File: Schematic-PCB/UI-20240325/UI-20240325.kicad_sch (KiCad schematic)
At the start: 18 parts, among them J1 Conn_01x10_Pin, SW1 SW_SPDT, SW2 SW_SPDT, SW3 SW_Push, SW5 SW_Push

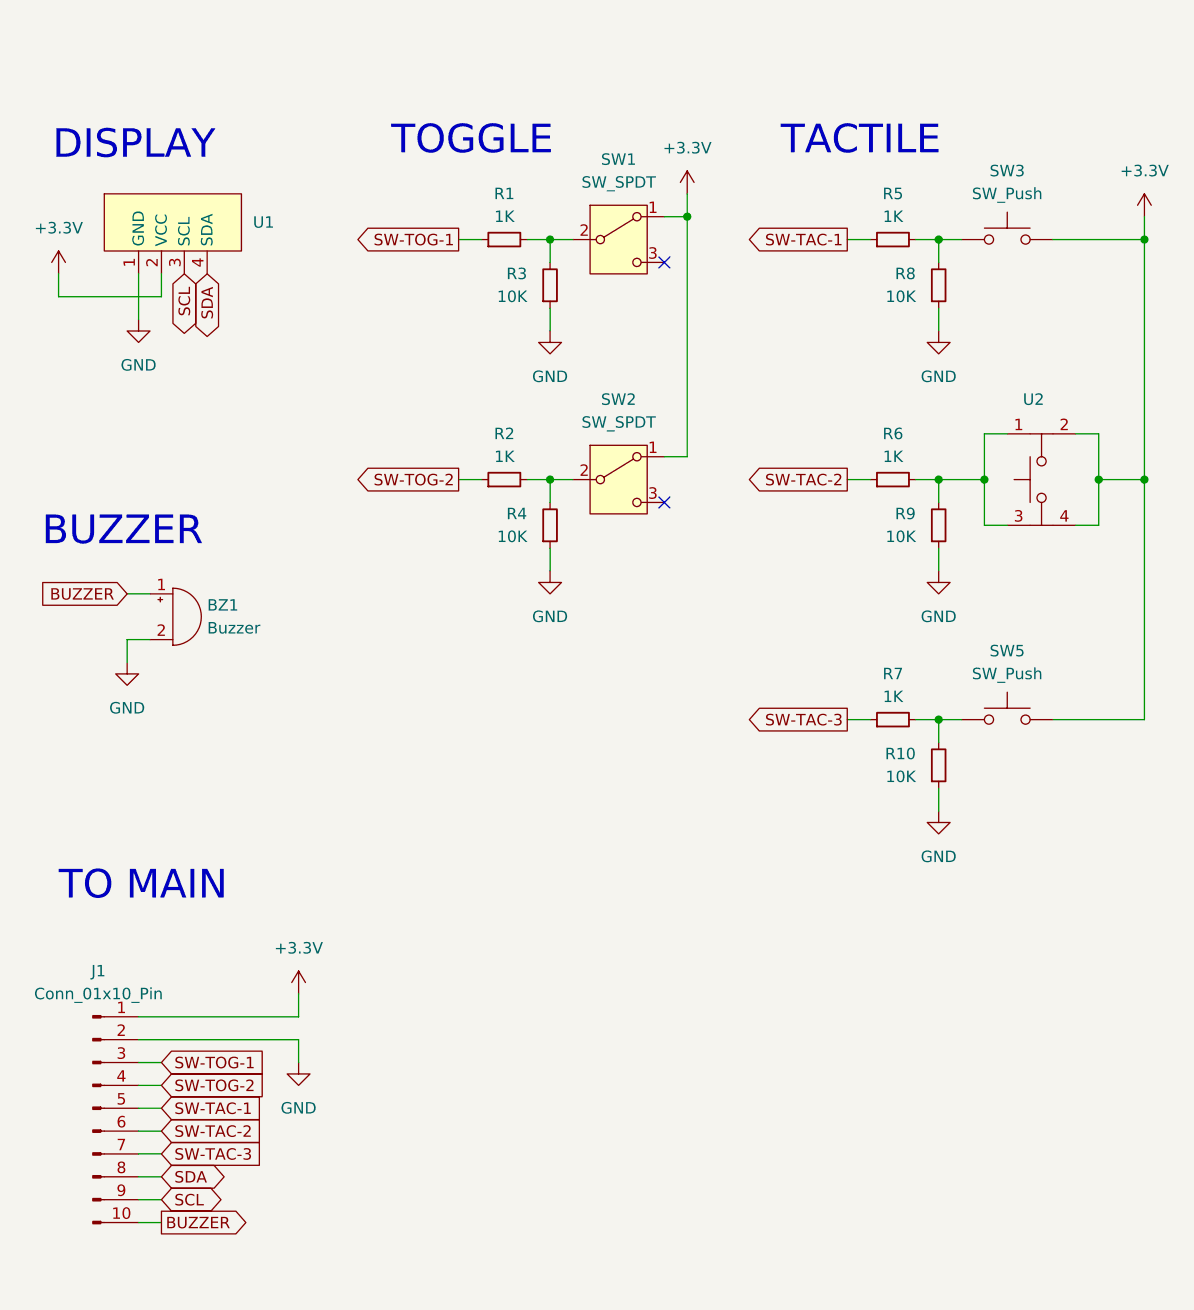
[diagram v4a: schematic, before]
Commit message: UI基板の回路図とPCBを作成しなおした
DRよろしく
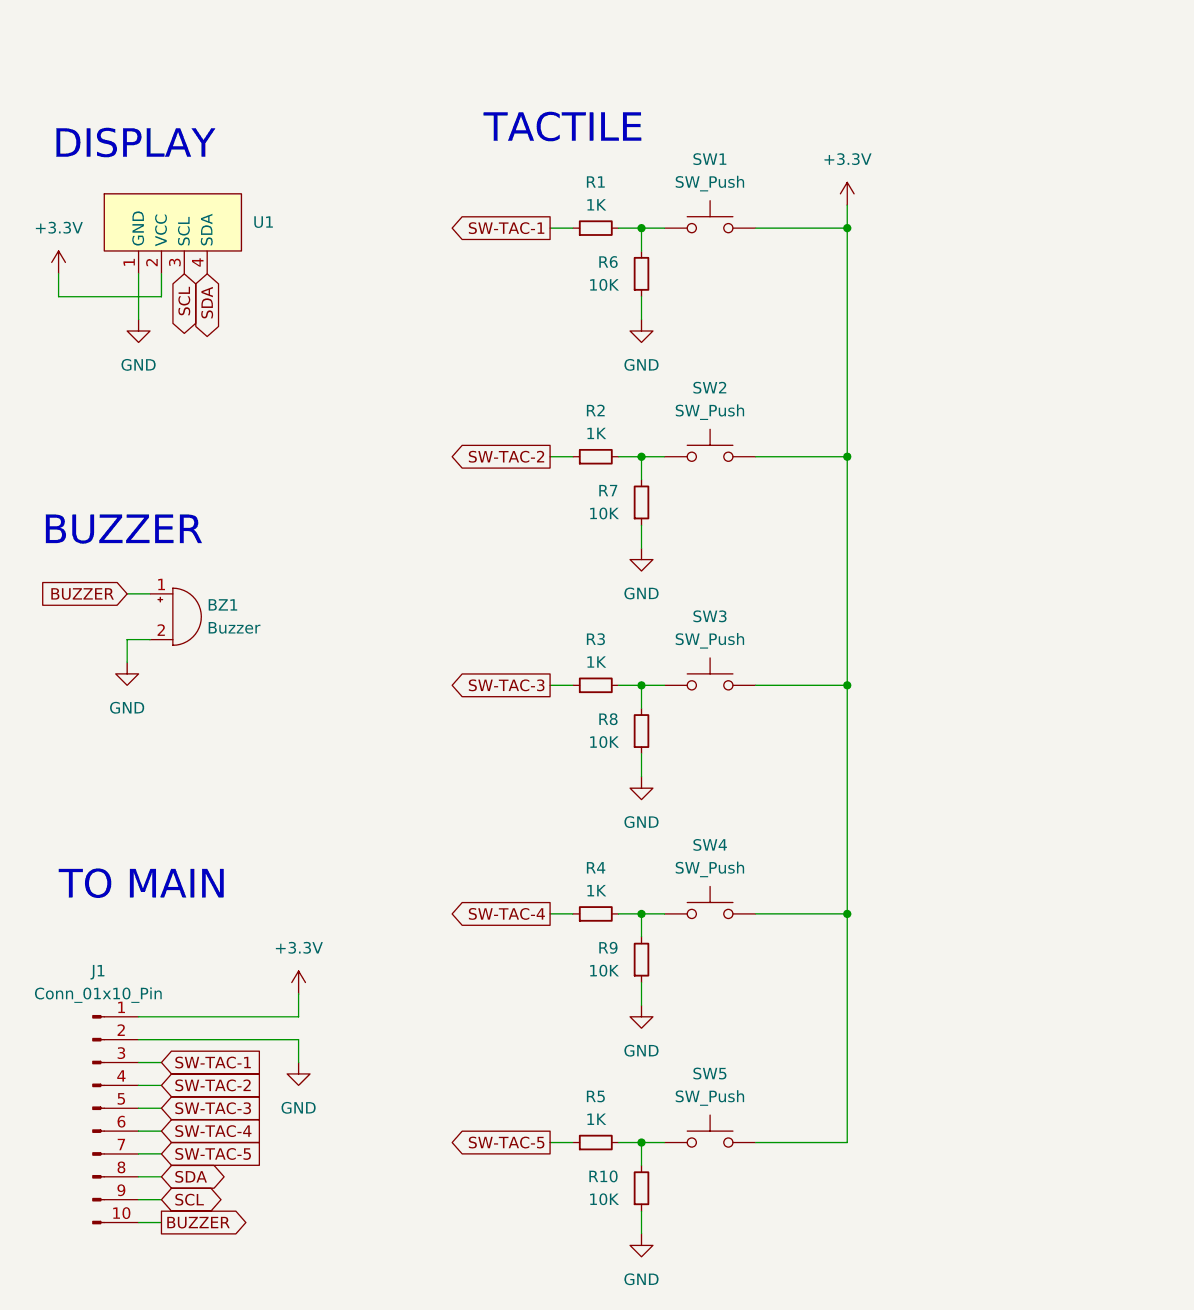
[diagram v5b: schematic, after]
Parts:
- removed R1, R6: 1K, Resistor_SMD:R_0603_1608Metric, symbol Device:R_Small
- removed SW1, SW2: SW_SPDT, @2024-UI:2MS1-T1-B4-VS2-Q-E-S, symbol Switch:SW_SPDT
- removed U2: ~, @2024-UI:TVGP01-G73BB, symbol @2024-UI:TVGP01-G73BB
- added R5: 1K, Resistor_SMD:R_0603_1608Metric, symbol Device:R_Small
- added R8: 10K, Resistor_SMD:R_0603_1608Metric, symbol Device:R_Small
- added SW2, SW3, SW4: SW_Push, @2024-UI:TVBP06-B043C, symbol Switch:SW_Push
- R3, R4: value 10K -> 1K
- R7: value 1K -> 10K
- renumbered R5 to R1, R8 to R6, SW3 to SW1
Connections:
- net SW-TOG-1 is gone; now on net SW-TAC-1: J1.3 (Pin_3)
- net SW-TOG-2 is gone; now on net SW-TAC-2: J1.4 (Pin_4), R2.1
- net +3.3V: now also SW2.2, SW3.2, SW4.2
- net GND: now also R7.1, R8.1; no longer R3.1, R4.1
- net SW-TAC-1: no longer J1.5 (Pin_5)
- net SW-TAC-2: no longer J1.6 (Pin_6)
- net SW-TAC-3: now also J1.5 (Pin_5), R3.1; no longer J1.7 (Pin_7), R7.1
- net at R10.2, SW5.1: now also R5.2; no longer R7.2
- net at R3.2: now also R8.2, SW3.1
- net at R2.2: now also R7.2, SW2.1; no longer R4.2
- net at R9.2: now also R4.2, SW4.1
- new net SW-TAC-4: J1.6 (Pin_6), R4.1
- new net SW-TAC-5: J1.7 (Pin_7), R5.1
- no-connect marks 2 -> 0
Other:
- note removed: "TOGGLE"
- moved on the sheet: R1, R6, SW1

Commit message: ラインセンサ基板のPCBを更新
ちょっと停滞中... ヘルプ求む、
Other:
- moved on the sheet: BZ1, J1, R1, R10, R2, R3, R4, R5, R6, R7, R8, R9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

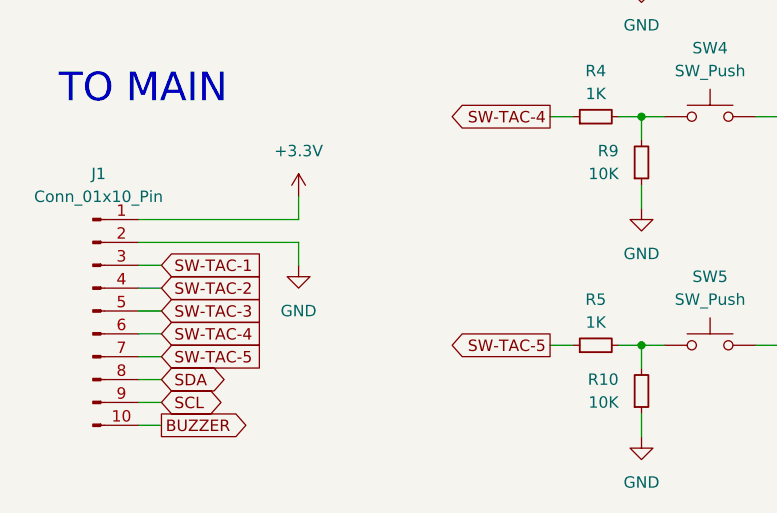
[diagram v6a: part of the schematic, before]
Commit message: UI基板の配線がねじれてしまう問題を解決した
ピンアサインに変更有、ピンアサイン図の変更が必要
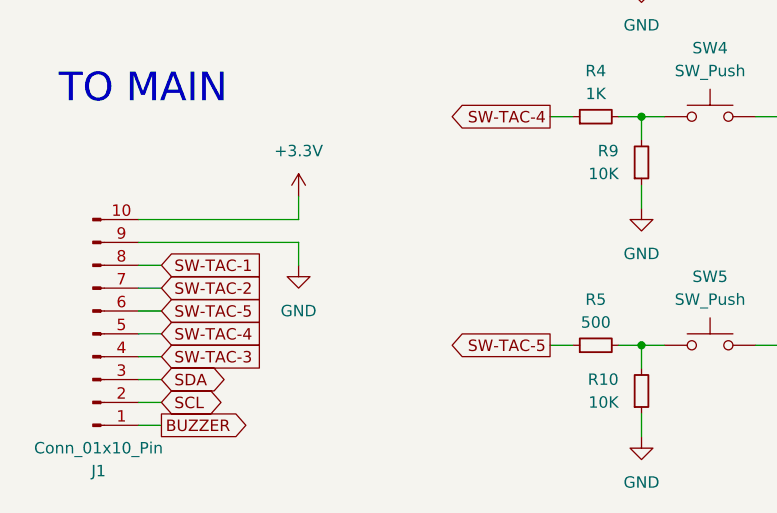
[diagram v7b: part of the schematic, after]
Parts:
- BZ1: footprint @2024-UI:PKM13EPYH4000-A0 -> @2024TOINIOT2-UI:PKM13EPYH4000-A0
- R5: value 1K -> 500
- SW1, SW2, SW3, SW4, SW5: footprint @2024-UI:TVBP06-B043C -> @2024TOINIOT2-UI:TVBP06-B043C
- U1: footprint @2024-UI:Display -> @2024TOINIOT2-UI:Display
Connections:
- net +3.3V: now also J1.10 (Pin_10); no longer J1.1 (Pin_1)
- net BUZZER: now also J1.1 (Pin_1); no longer J1.10 (Pin_10)
- net GND: now also J1.9 (Pin_9); no longer J1.2 (Pin_2)
- net SCL: now also J1.2 (Pin_2); no longer J1.9 (Pin_9)
- net SDA: now also J1.3 (Pin_3); no longer J1.8 (Pin_8)
- net SW-TAC-1: now also J1.8 (Pin_8); no longer J1.3 (Pin_3)
- net SW-TAC-2: now also J1.7 (Pin_7); no longer J1.4 (Pin_4)
- net SW-TAC-3: now also J1.4 (Pin_4); no longer J1.5 (Pin_5)
- net SW-TAC-4: now also J1.5 (Pin_5); no longer J1.6 (Pin_6)
- net SW-TAC-5: now also J1.6 (Pin_6); no longer J1.7 (Pin_7)
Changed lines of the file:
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@@
 	(global_label "SW-TAC-5"
 		(shape input)
-		(at 43.18 143.51 0)
+		(at 43.18 138.43 0)
 		(fields_autoplaced yes)
 		(effects
@@
 		)
 		(property "Intersheetrefs" "${INTERSHEET_REFS}"
-			(at 55.2496 143.51 0)
+			(at 55.2496 138.43 0)
 			(effects
 				(font
@@
 	(global_label "SW-TAC-3"
 		(shape input)
-		(at 43.18 138.43 0)
+		(at 43.18 143.51 0)
 		(fields_autoplaced yes)
 		(effects
@@
 		)
 		(property "Intersheetrefs" "${INTERSHEET_REFS}"
-			(at 55.2496 138.43 0)
+			(at 55.2496 143.51 0)
 			(effects
 				(font
@@
 			)
 		)
-		(property "Footprint" "@2024-UI:TVBP06-B043C"
+		(property "Footprint" "@2024TOINIOT2-UI:TVBP06-B043C"
 			(at 104.14 35.56 0)
 			(effects
@@
 			)
 		)
-		(property "Footprint" "@2024-UI:TVBP06-B043C"
+		(property "Footprint" "@2024TOINIOT2-UI:TVBP06-B043C"
 			(at 104.14 137.16 0)
 			(effects
@@
 	(symbol
 		(lib_id "Connector:Conn_01x10_Pin")
-		(at 35.56 138.43 0)
-		(unit 1)
-		(exclude_from_sim no)
-		(in_bom yes)
-		(on_board yes)
-		(dnp no)
-		(fields_autoplaced yes)
+		(at 35.56 140.97 0)
+		(mirror x)
+		(unit 1)
+		(exclude_from_sim no)
+		(in_bom yes)
+		(on_board yes)
+		(dnp no)
 		(property "Reference" "J1"
-			(at 36.195 123.19 0)
+			(at 36.195 156.21 0)
 			(effects
 				(font
@@
 		)
 		(property "Value" "Conn_01x10_Pin"
-			(at 36.195 125.73 0)
+			(at 36.195 153.67 0)
 			(effects
 				(font
@@
 		)
 		(property "Footprint" "Connector_JST:JST_XH_B10B-XH-A_1x10_P2.50mm_Vertical"
-			(at 35.56 138.43 0)
+			(at 35.56 140.97 0)
 			(effects
 				(font
@@
 		)
 		(property "Datasheet" "~"
-			(at 35.56 138.43 0)
+			(at 35.56 140.97 0)
 			(effects
 				(font
@@
 		)
 		(property "Description" "Generic connector, single row, 01x10, script generated"
-			(at 35.56 138.43 0)
+			(at 35.56 140.97 0)
 			(effects
 				(font
@@
 			)
 		)
-		(property "Footprint" "@2024-UI:Display"
+		(property "Footprint" "@2024TOINIOT2-UI:Display"
 			(at 44.45 29.718 0)
 			(effects
@@
 			)
 		)
-		(property "Footprint" "@2024-UI:TVBP06-B043C"
+		(property "Footprint" "@2024TOINIOT2-UI:TVBP06-B043C"
 			(at 104.14 86.36 0)
 			(effects
@@
 			)
 		)
-		(property "Footprint" "@2024-UI:PKM13EPYH4000-A0"
+		(property "Footprint" "@2024TOINIOT2-UI:PKM13EPYH4000-A0"
 			(at 43.815 81.28 90)
 			(effects
@@
 			)
 		)
-		(property "Footprint" "@2024-UI:TVBP06-B043C"
+		(property "Footprint" "@2024TOINIOT2-UI:TVBP06-B043C"
 			(at 104.14 60.96 0)
 			(effects
@@
 			)
 		)
-		(property "Value" "1K"
+		(property "Value" "500"
 			(at 91.44 139.7 90)
 			(effects
@@
 			)
 		)
-		(property "Footprint" "@2024-UI:TVBP06-B043C"
+		(property "Footprint" "@2024TOINIOT2-UI:TVBP06-B043C"
 			(at 104.14 111.76 0)
 			(effects

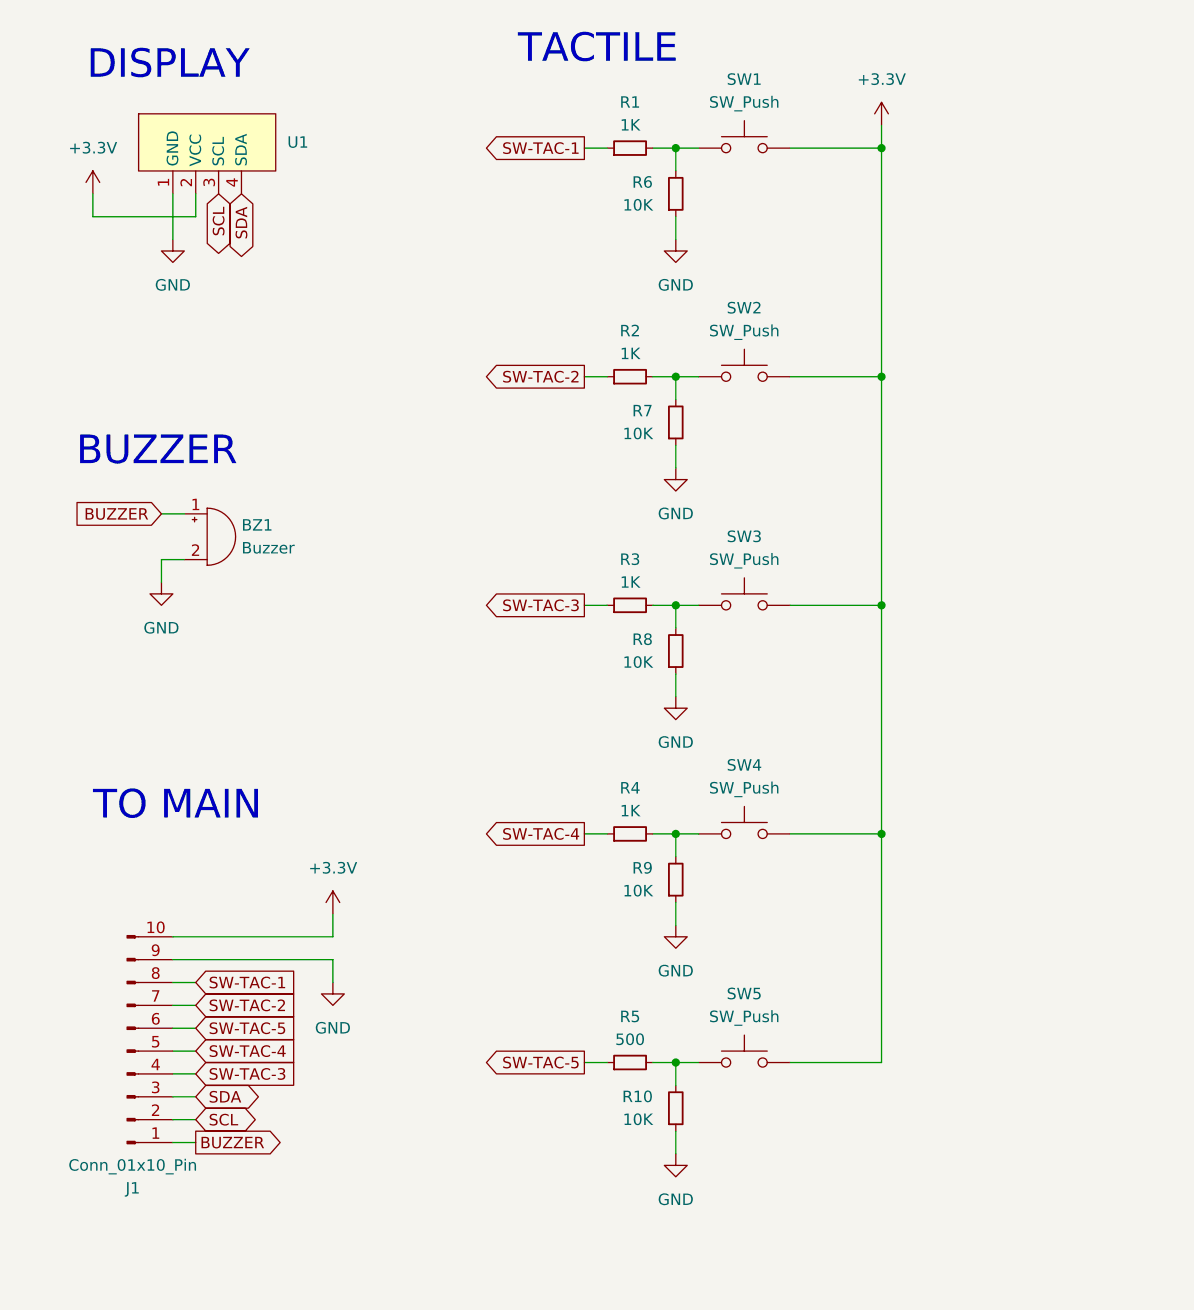
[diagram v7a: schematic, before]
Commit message: UI基板を修正/MD基板を修正/メイン基板を作り直し （ver.002）
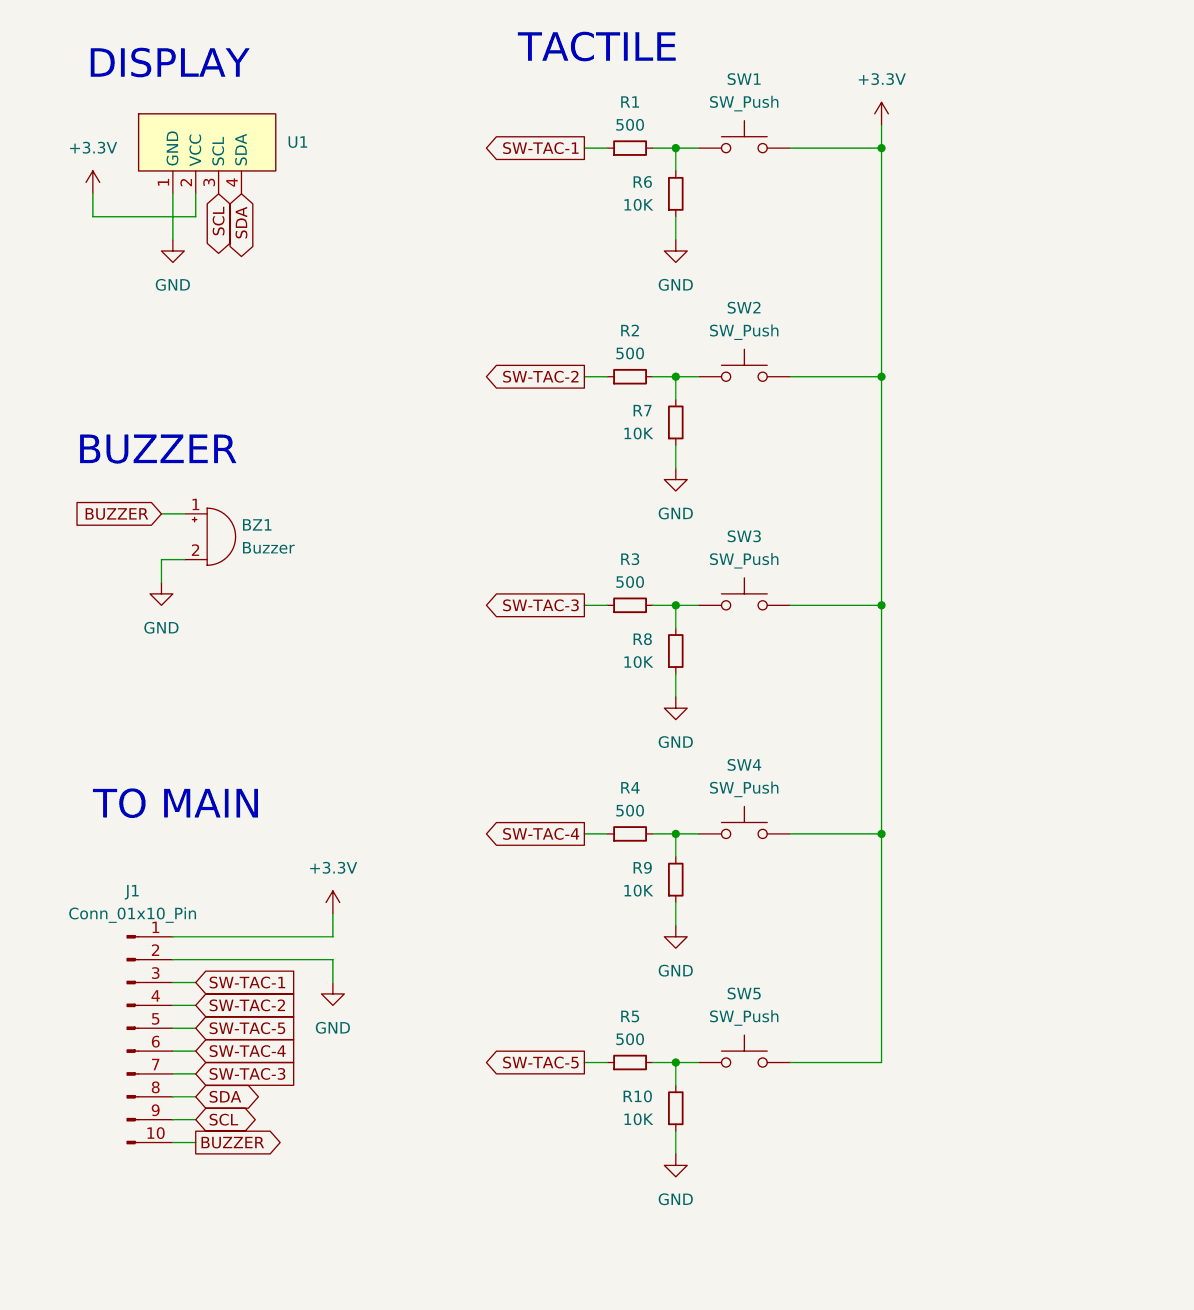
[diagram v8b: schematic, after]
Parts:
- R1, R2, R3, R4: value 1K -> 500
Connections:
- net +3.3V: now also J1.1 (Pin_1); no longer J1.10 (Pin_10)
- net BUZZER: now also J1.10 (Pin_10); no longer J1.1 (Pin_1)
- net GND: now also J1.2 (Pin_2); no longer J1.9 (Pin_9)
- net SCL: now also J1.9 (Pin_9); no longer J1.2 (Pin_2)
- net SDA: now also J1.8 (Pin_8); no longer J1.3 (Pin_3)
- net SW-TAC-1: now also J1.3 (Pin_3); no longer J1.8 (Pin_8)
- net SW-TAC-2: now also J1.4 (Pin_4); no longer J1.7 (Pin_7)
- net SW-TAC-3: now also J1.7 (Pin_7); no longer J1.4 (Pin_4)
- net SW-TAC-4: now also J1.6 (Pin_6); no longer J1.5 (Pin_5)
- net SW-TAC-5: now also J1.5 (Pin_5); no longer J1.6 (Pin_6)
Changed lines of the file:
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@@
 			)
 		)
-		(property "Value" "1K"
+		(property "Value" "500"
 			(at 91.44 38.1 90)
 			(effects
@@
 			)
 		)
-		(property "Value" "1K"
+		(property "Value" "500"
 			(at 91.44 88.9 90)
 			(effects
@@
 	(symbol
 		(lib_id "Connector:Conn_01x10_Pin")
-		(at 35.56 140.97 0)
-		(mirror x)
+		(at 35.56 138.43 0)
 		(unit 1)
 		(exclude_from_sim no)
@@
 		(dnp no)
 		(property "Reference" "J1"
-			(at 36.195 156.21 0)
+			(at 36.195 123.19 0)
 			(effects
 				(font
@@
 		)
 		(property "Value" "Conn_01x10_Pin"
-			(at 36.195 153.67 0)
+			(at 36.195 125.73 0)
 			(effects
 				(font
@@
 		)
 		(property "Footprint" "Connector_JST:JST_XH_B10B-XH-A_1x10_P2.50mm_Vertical"
-			(at 35.56 140.97 0)
+			(at 35.56 138.43 0)
 			(effects
 				(font
@@
 		)
 		(property "Datasheet" "~"
-			(at 35.56 140.97 0)
+			(at 35.56 138.43 0)
 			(effects
 				(font
@@
 		)
 		(property "Description" "Generic connector, single row, 01x10, script generated"
-			(at 35.56 140.97 0)
+			(at 35.56 138.43 0)
 			(effects
 				(font
@@
 			)
 		)
-		(property "Value" "1K"
+		(property "Value" "500"
 			(at 91.44 63.5 90)
 			(effects
@@
 			)
 		)
-		(property "Value" "1K"
+		(property "Value" "500"
 			(at 91.44 114.3 90)
 			(effects
